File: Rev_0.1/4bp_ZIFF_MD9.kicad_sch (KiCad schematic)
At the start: 134 parts, among them CN1 MD-90SM_MD2, IC1 THS7374IPWR, IC2 TL974, J1 SMD_Conn_01x01, J2 SMD_Conn_01x01, J3 SolderJumper_3_Open, J4 SolderJumper_2_Open, J5 SMD_Conn_01x01, J6 SMD_Conn_01x01, M1PU1 SolderJumper_2_Open, P1 SMD_Conn_01x01, U1 AD725, Y1 HCM4917734475ABJT, Y2 HCM4914318180BBKT

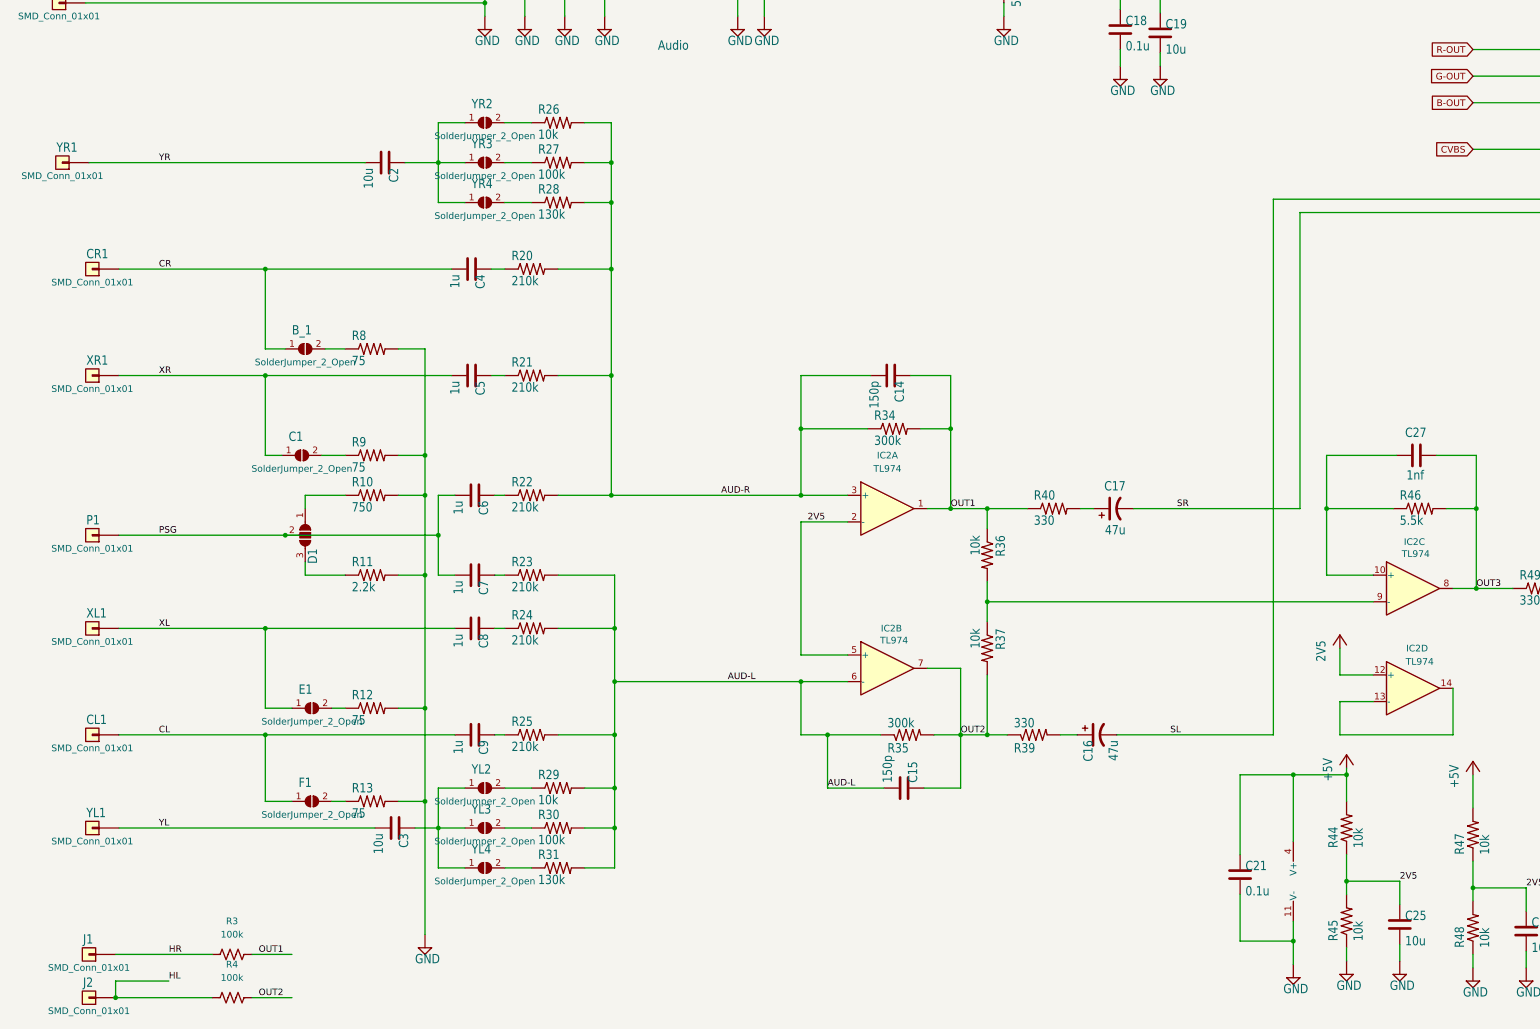
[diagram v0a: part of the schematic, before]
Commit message: Added 2nd set of jumbers for resistor isolation
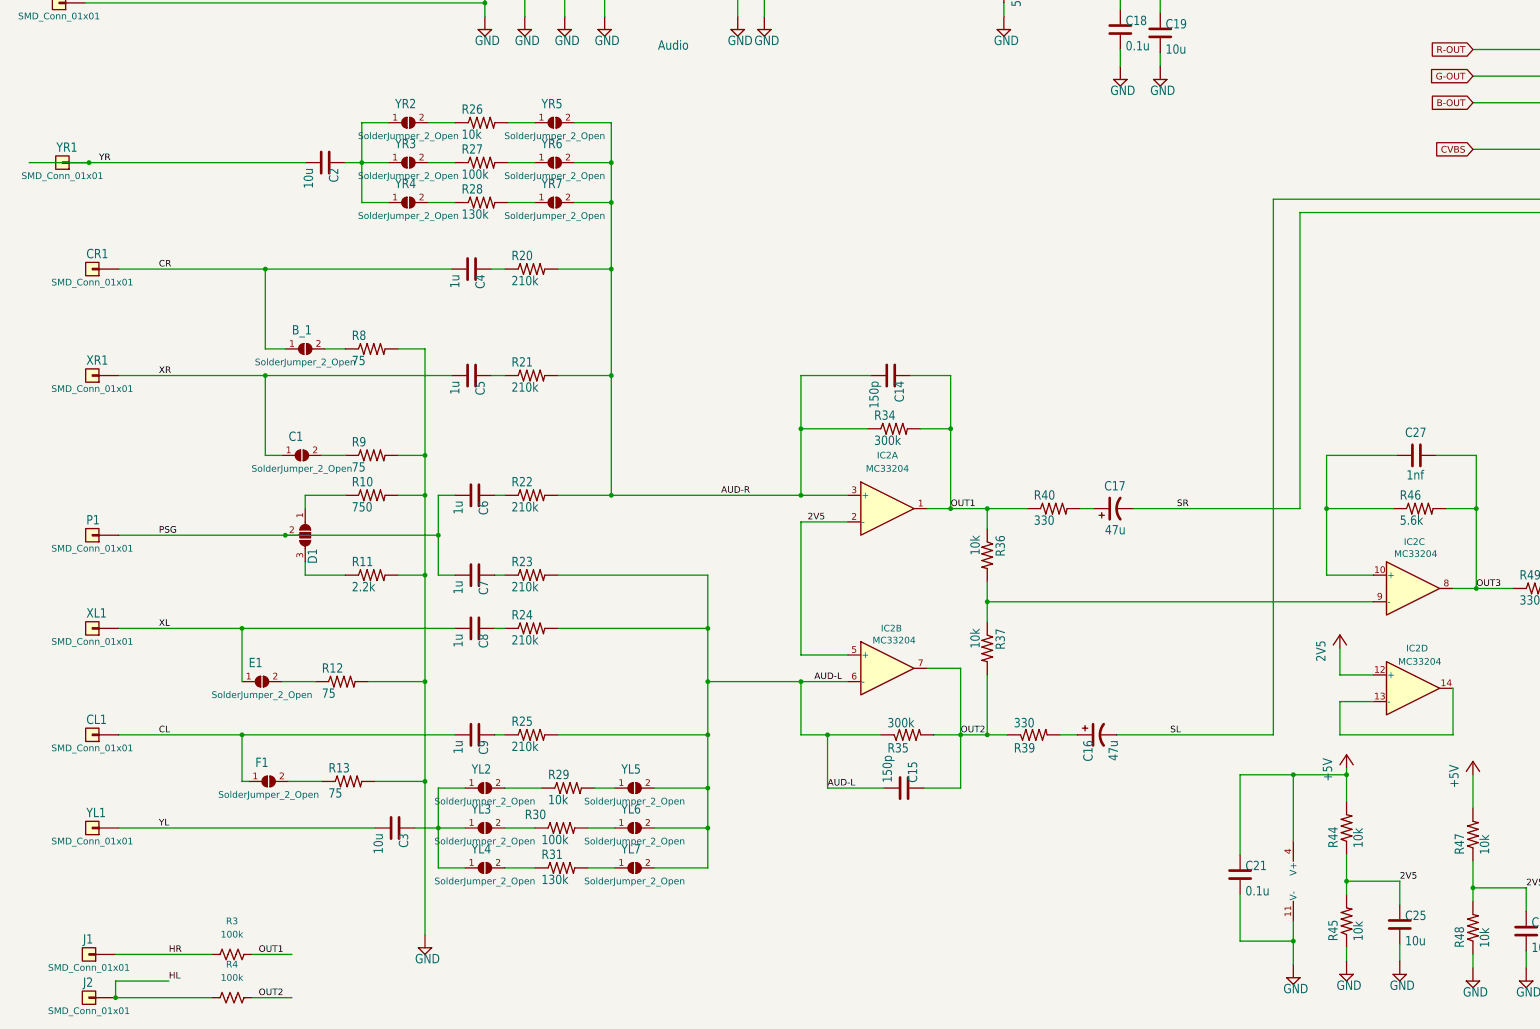
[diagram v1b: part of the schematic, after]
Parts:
- added YL5, YL6, YL7, YR5, YR6, YR7: SolderJumper_2_Open, Jumper:SolderJumper-2_P1.3mm_Open_RoundedPad1.0x1.5mm, symbol Jumper:SolderJumper_2_Open
- IC2: value TL974 -> MC33204
- R46: value 5.5k -> 5.6k
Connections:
- net AUD-L: now also YL5.2 (B), YL6.2 (B), YL7.2 (B); no longer R29.2, R30.2, R31.2
- net AUD-R: now also YR5.2 (B), YR6.2 (B), YR7.2 (B); no longer R26.2, R27.2, R28.2
- new net: R27.2, YR6.1 (A)
- new net: R31.2, YL7.1 (A)
- new net: R26.2, YR5.1 (A)
- new net: R28.2, YR7.1 (A)
- new net: R30.2, YL6.1 (A)
- new net: R29.2, YL5.1 (A)
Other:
- moved on the sheet: C2, E1, F1, R12, R13, R26, R27, R28, R29, R30, R31, YR2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
